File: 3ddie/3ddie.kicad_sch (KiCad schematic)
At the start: 54 parts, among them J1 USB4105-GF-A, U1 W25Q128JV, U2 RP2040, U3 BoostedElectrodes, U4 MCP1702T-3302E_CB, U5 MGC3130-I{slash}MQ, U6 MGC3130-I/MQ, U7 MCP1416R, Y1 12MHz

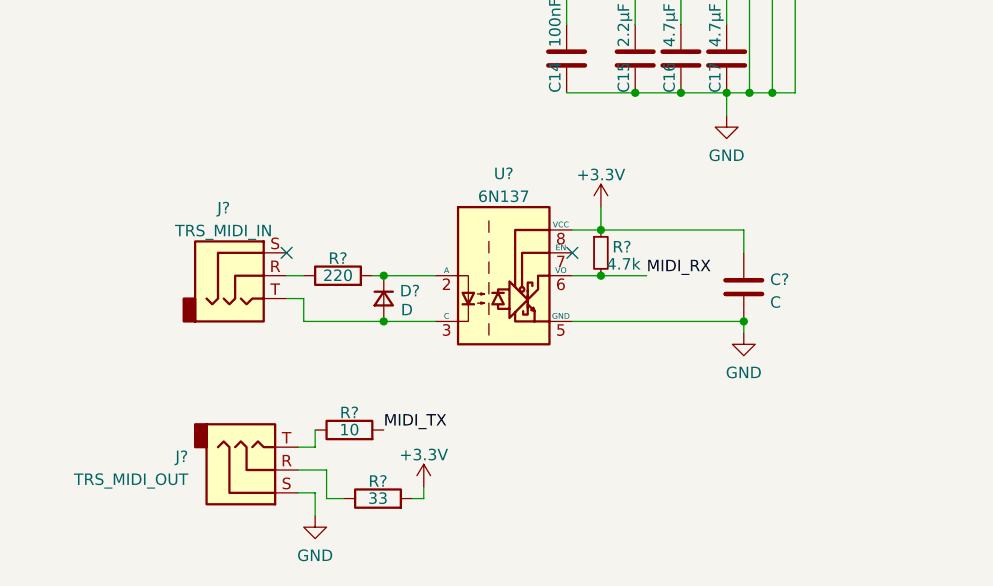
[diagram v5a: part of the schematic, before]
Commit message: annotate symbols, add value to optocoupler bypass cap
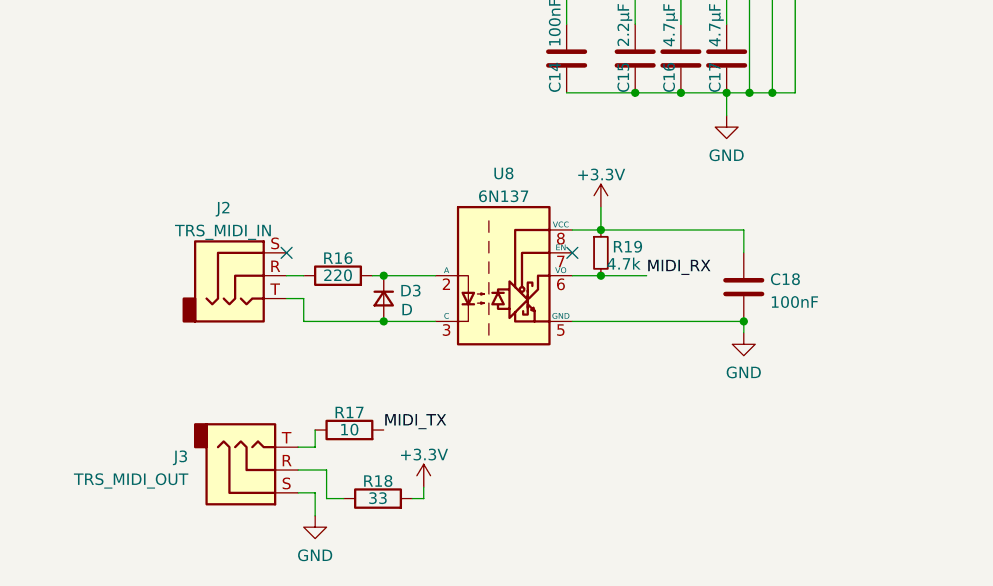
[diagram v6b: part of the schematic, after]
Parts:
- C18: renamed from C?; value C -> 100nF
- gave numbers to parts that had none: 8

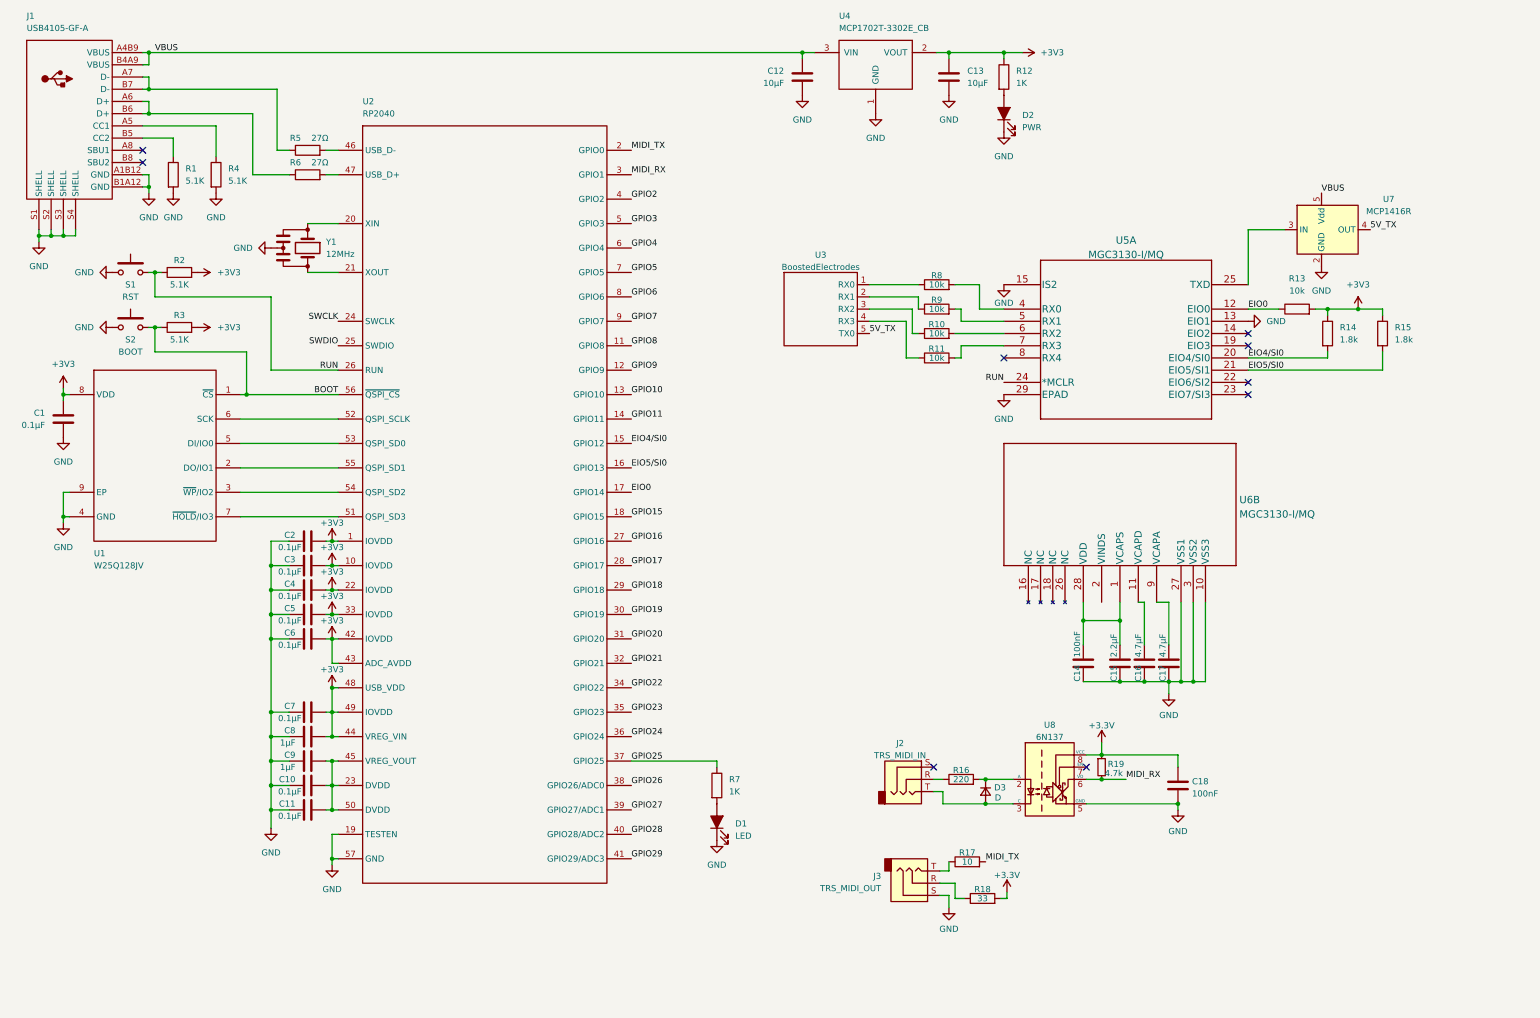
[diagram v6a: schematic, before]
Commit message: update component value formatting for consistency
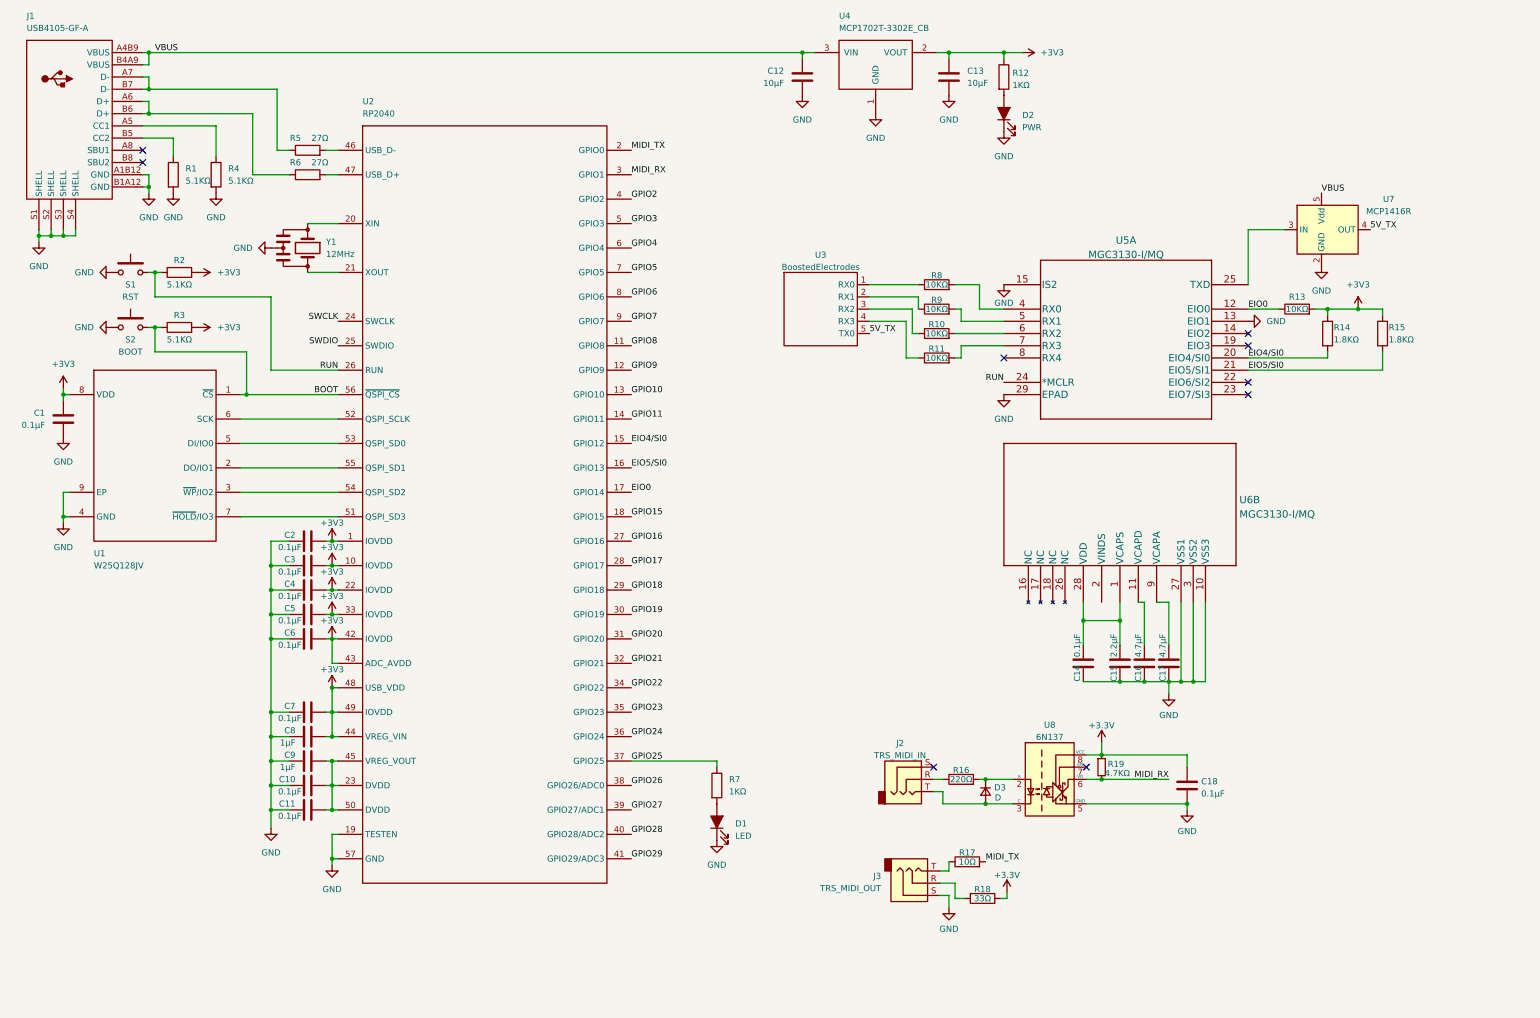
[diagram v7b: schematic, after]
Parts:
- C14, C18: value 100nF -> 0.1μF
- R1, R2, R3, R4: value 5.1K -> 5.1KΩ
- R10, R11, R13, R8, R9: value 10k -> 10KΩ
- R12, R7: value 1K -> 1KΩ
- R14, R15: value 1.8k -> 1.8KΩ
- R16: value 220 -> 220Ω
- R17: value 10 -> 10Ω
- R18: value 33 -> 33Ω
- R19: value 4.7k -> 4.7KΩ
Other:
- moved on the sheet: C18

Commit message: fix symbol annotations
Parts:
- U4: renamed from U5; value MGC3130-I/MQ -> MGC3130-I/MQ
- renumbered U4 to U3, U6 to U4, U7 to U5, U8 to U6, U3 to U7
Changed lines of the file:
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@@
   (symbol (lib_id "3ddie:BoostedElectrodes") (at 187.96 74.93 0) (unit 1)
     (in_bom yes) (on_board yes) (fields_autoplaced)
-    (property "Reference" "U3" (id 0) (at 187.96 71.281 0))
+    (property "Reference" "U7" (id 0) (at 187.96 71.281 0))
     (property "Value" "BoostedElectrodes" (id 1) (at 187.96 73.8179 0))
     (property "Footprint" "" (id 2) (at 187.96 74.93 0)
@@
   (symbol (lib_id "Driver_FET:MCP1416R") (at 292.1 66.04 0) (unit 1)
     (in_bom yes) (on_board yes)
-    (property "Reference" "U7" (id 0) (at 306.07 59.69 0))
+    (property "Reference" "U5" (id 0) (at 306.07 59.69 0))
     (property "Value" "MCP1416R" (id 1) (at 306.07 62.23 0))
     (property "Footprint" "Package_TO_SOT_SMD:SOT-23-5" (id 2) (at 292.1 76.2 0)
@@
   (symbol (lib_name "MGC3130-I{brace}slash}MQ_1") (lib_id "3ddie:MGC3130-I{brace}slash}MQ") (at 231.14 143.51 90) (unit 2)
     (in_bom yes) (on_board yes) (fields_autoplaced)
-    (property "Reference" "U6" (id 0) (at 275.0185 122.2138 90)
+    (property "Reference" "U4" (id 0) (at 275.0185 122.2138 90)
       (effects (font (size 1.524 1.524)) (justify right))
     )
@@
   (symbol (lib_id "3ddie:MGC3130-I{brace}slash}MQ") (at 226.06 77.47 0) (unit 1)
     (in_bom yes) (on_board yes) (fields_autoplaced)
-    (property "Reference" "U5" (id 0) (at 251.46 68.2424 0)
+    (property "Reference" "U4" (id 0) (at 251.46 68.2424 0)
       (effects (font (size 1.524 1.524)))
     )
-    (property "Value" "MGC3130-I{slash}MQ" (id 1) (at 251.46 71.2358 0)
+    (property "Value" "MGC3130-I/MQ" (id 1) (at 251.46 71.2358 0)
       (effects (font (size 1.524 1.524)))
     )
@@
   (symbol (lib_id "Isolator:6N137") (at 235.585 180.34 0) (unit 1)
     (in_bom yes) (on_board yes) (fields_autoplaced)
-    (property "Reference" "U8" (id 0) (at 235.585 169.0202 0))
+    (property "Reference" "U6" (id 0) (at 235.585 169.0202 0))
     (property "Value" "6N137" (id 1) (at 235.585 171.5571 0))
     (property "Footprint" "Package_DIP:DIP-8_W7.62mm" (id 2) (at 235.585 193.04 0)
@@
   (symbol (lib_id "Eclectronics:MCP1702T-3302E_CB") (at 199.39 31.75 0) (unit 1)
     (in_bom yes) (on_board yes)
-    (property "Reference" "U4" (id 0) (at 191.77 21.59 0)
+    (property "Reference" "U3" (id 0) (at 191.77 21.59 0)
       (effects (font (size 1.27 1.27)) (justify left))
     )
@@
       (reference "U2") (unit 1) (value "RP2040") (footprint "Eclectronics:RP2040")
     )
+    (path "/e5364cca-4794-4d2b-8070-6ef7bfc147df"
+      (reference "U3") (unit 1) (value "MCP1702T-3302E_CB") (footprint "Package_TO_SOT_SMD:SOT-23")
+    )
+    (path "/a9329e99-609f-4c39-a02d-48cc774ada87"
+      (reference "U4") (unit 1) (value "MGC3130-I/MQ") (footprint "QFN28_5X5MQ_MCH")
+    )
+    (path "/5936d240-6102-4439-994a-788eb8b3c026"
+      (reference "U4") (unit 2) (value "MGC3130-I/MQ") (footprint "QFN28_5X5MQ_MCH")
+    )
+    (path "/15b2a124-1eb8-4d1a-932b-488f6e69f5b6"
+      (reference "U5") (unit 1) (value "MCP1416R") (footprint "Package_TO_SOT_SMD:SOT-23-5")
+    )
+    (path "/bca2ac86-8d9c-4b32-ab1d-2258827622a1"
+      (reference "U6") (unit 1) (value "6N137") (footprint "Package_DIP:DIP-8_W7.62mm")
+    )
     (path "/0030390e-c97e-47e6-97d2-f7c983a931fc"
-      (reference "U3") (unit 1) (value "BoostedElectrodes") (footprint "")
-    )
-    (path "/e5364cca-4794-4d2b-8070-6ef7bfc147df"
-      (reference "U4") (unit 1) (value "MCP1702T-3302E_CB") (footprint "Package_TO_SOT_SMD:SOT-23")
-    )
-    (path "/a9329e99-609f-4c39-a02d-48cc774ada87"
-      (reference "U5") (unit 1) (value "MGC3130-I{slash}MQ") (footprint "QFN28_5X5MQ_MCH")
-    )
-    (path "/5936d240-6102-4439-994a-788eb8b3c026"
-      (reference "U6") (unit 2) (value "MGC3130-I/MQ") (footprint "QFN28_5X5MQ_MCH")
-    )
-    (path "/15b2a124-1eb8-4d1a-932b-488f6e69f5b6"
-      (reference "U7") (unit 1) (value "MCP1416R") (footprint "Package_TO_SOT_SMD:SOT-23-5")
-    )
-    (path "/bca2ac86-8d9c-4b32-ab1d-2258827622a1"
-      (reference "U8") (unit 1) (value "6N137") (footprint "Package_DIP:DIP-8_W7.62mm")
+      (reference "U7") (unit 1) (value "BoostedElectrodes") (footprint "")
     )
     (path "/5959d32e-5374-437a-b818-10a8297a1179"
